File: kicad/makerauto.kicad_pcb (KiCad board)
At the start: 2 copper layers, 53.8 x 73.9 mm, 2 parts

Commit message: initial layout
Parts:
- removed the G*** at (0.00, 0.00)
- added BT1: BATT_HOLDER, makerauto:cr2032_02, B.Cu at (0.00, -9.50)
- added D1: Red, makerauto:LED-5MM, F.Cu at (0.00, 13.0)
- added D2: Grn, makerauto:LED-5MM, F.Cu at (15.0, 0.00)
- added D3: Blu, makerauto:LED-5MM, F.Cu at (-15.0, 0.00)
- added LOGO1: OPEN_HARDWARE_1, makerauto:Logo_silk_OSHW_6x6mm, B.Cu at (0.00, 23.0)
- added P1: Logo_MA, makerauto:ma_logo, F.Cu at (0.00, 0.00)
- added P2: Mirror, makerauto:MTG_3mm, F.Cu at (-24.0, -20.0)
- added P3: Mirror, makerauto:MTG_3mm, F.Cu at (24.0, -20.0)
- added P4: Pin, makerauto:MTG_0mm8, F.Cu at (-4.50, -31.0)
- added P5: Pin, makerauto:MTG_0mm8, F.Cu at (4.50, -35.0)
- added P6: Pin, makerauto:MTG_0mm8, F.Cu at (-4.50, -35.0)
- added P7: Pin, makerauto:MTG_0mm8, F.Cu at (4.50, -31.0)
- added R1: 47E, makerauto:r_0805, F.Cu at (0.00, 8.00)
- added R2: 47E, makerauto:r_0805, F.Cu at (11.0, 3.50)
- added R3: 47E, makerauto:r_0805, F.Cu at (-11.0, 3.50)
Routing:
- net /3V: track 0.00 -> 74.5 mm
- net /GND: track 0.00 -> 64.3 mm
- net /LED_grn: track 0.00 -> 10.1 mm
- net /LED_blu: track 0.00 -> 10.1 mm
- net /LED_red: track 0.00 -> 9.56 mm
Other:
- board size 53.8 x 73.9 mm -> 54.7 x 73.9 mm
- net class 0.5mm added: clearance 0.2, trace_width 0.5, via_dia 0.8, via_drill 0.4
- net class 1.0mm added: clearance 0.2, trace_width 1, via_dia 0.8, via_drill 0.4
- net class 1.5mm added: clearance 0.2, trace_width 1.5, via_dia 0.8, via_drill 0.4

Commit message: gerbers and pdf's generated
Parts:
- moved BT1 141.4 mm to (100.0, 90.5)
- moved D1 141.4 mm to (100.0, 113.0)
- moved D2 141.4 mm to (115.0, 100.0)
- moved D3 141.4 mm to (85.0, 100.0)
- moved G*** 141.4 mm to (67.1, 109.6)
- moved LOGO1 141.4 mm to (100.0, 123.0)
- moved P1 141.4 mm to (100.0, 100.0)
- moved P2 141.4 mm to (76.0, 80.0)
- moved P3 141.4 mm to (124.0, 80.0)
- moved P4 141.4 mm to (95.5, 69.0)
- moved P5 141.4 mm to (104.5, 65.0)
- moved P6 141.4 mm to (95.5, 65.0)
- moved P7 141.4 mm to (104.5, 69.0)
- moved R1 141.4 mm to (100.0, 108.0)
- moved R2 141.4 mm to (111.0, 103.5)
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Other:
- outline, holes or cut-outs redrawn

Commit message: added logos
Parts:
- added G***: LOGO, makerauto:logo_asylum, B.Cu at (88.5, 73.0)
- added G***: LOGO, makerauto:logo_autodesk, B.Cu at (112.5, 73.5)
- R1, R2, R3: moved to B.Cu
- moved LOGO1 9.00 mm to (100.0, 132.0)
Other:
- board text added: "Maker Auto : built with help from Maker's Asylum + Autodesk India"
- board text added: "SPACE FOR ETOK MARK AND CODE"
- board text added: "[+]"
- board text added: "[-]"
- board text added: "https://git.io/v6BwJ"

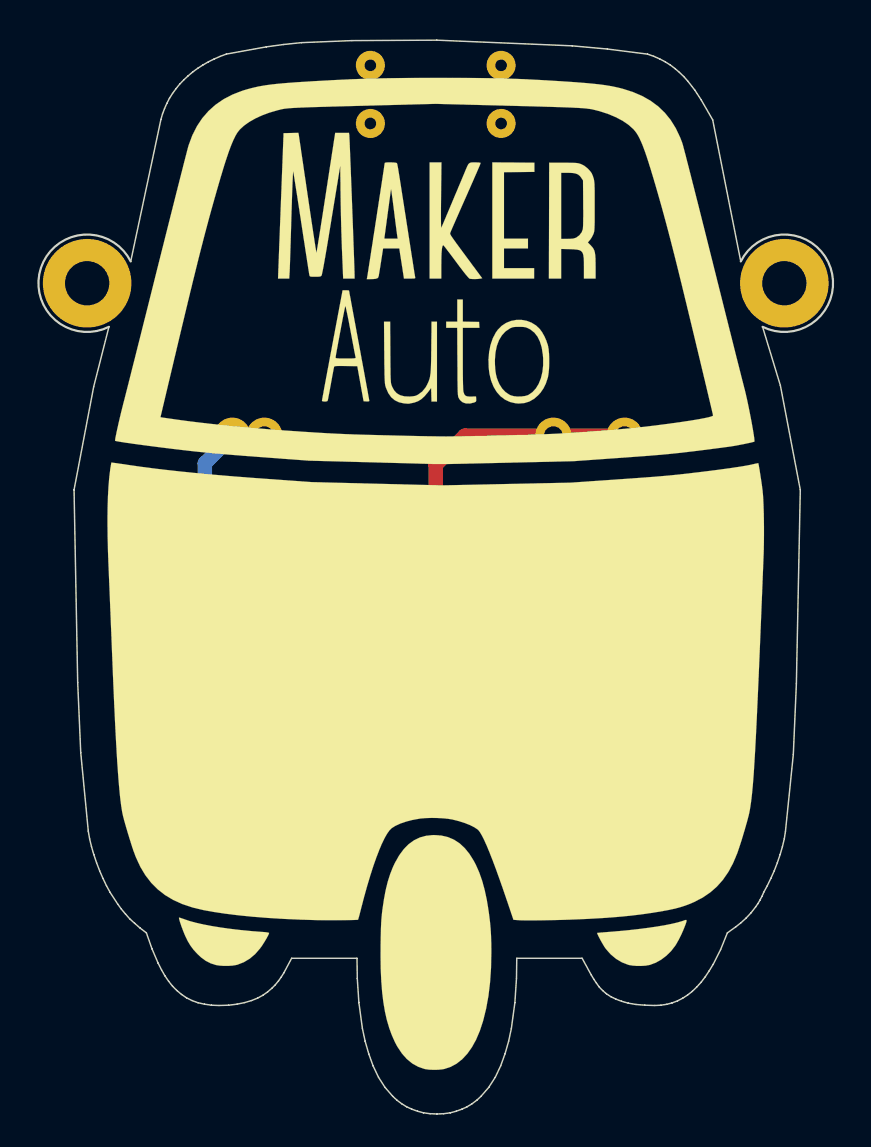
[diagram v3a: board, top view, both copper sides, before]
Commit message: added copper fill zones
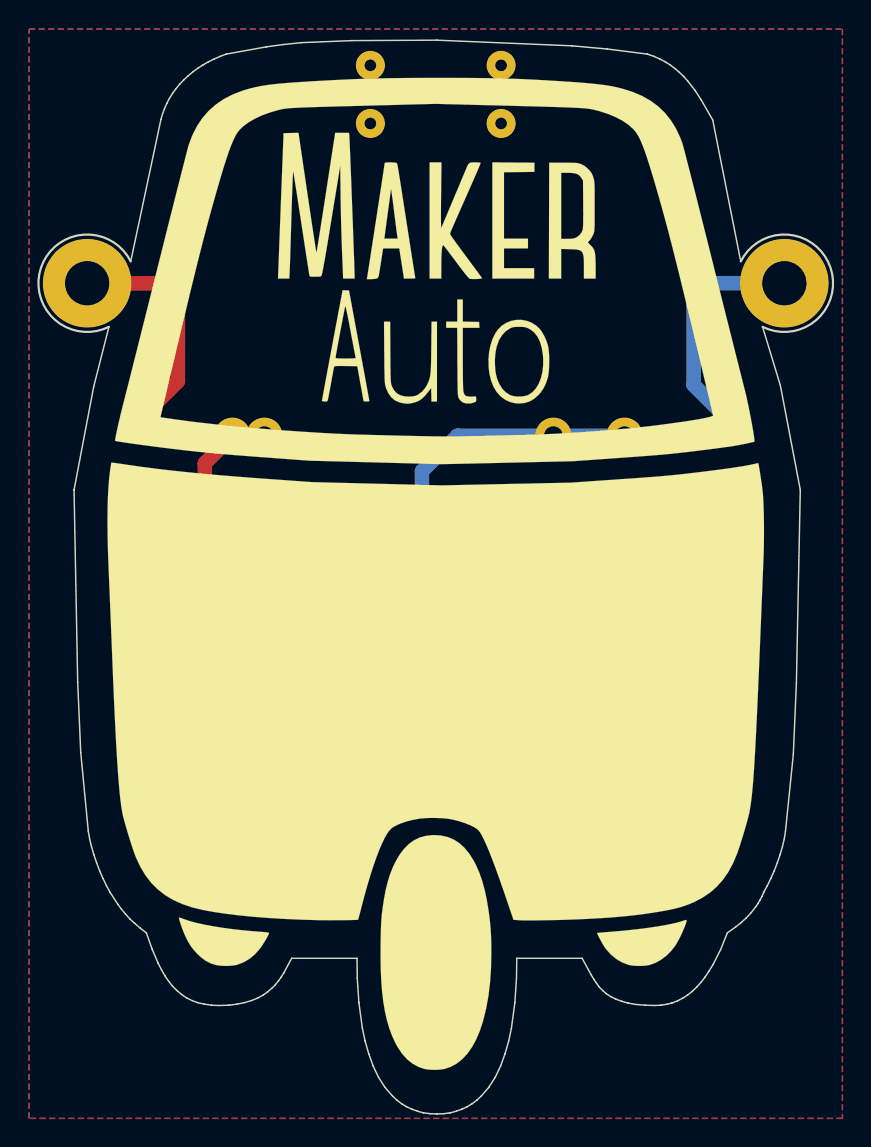
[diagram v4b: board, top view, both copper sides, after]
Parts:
- added P8: Pin, makerauto:MTG_0mm8, F.Cu at (79.5, 89.5)
- added P9: Pin, makerauto:MTG_0mm8, F.Cu at (120.5, 89.8)
- moved G*** 21.2 mm to (75.8, 129.0)
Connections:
- P2 pad 1: (no net) -> /TOP
- P3 pad 1: (no net) -> /BOT
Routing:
- net /TOP: track 0.00 -> 16.3 mm
- net /BOT: track 0.00 -> 16.3 mm
- net /LED_grn: track 10.1 -> 7.69 mm
- net /LED_blu: track 10.1 -> 7.69 mm
- net /LED_red: track 9.56 -> 7.24 mm
- net /GND: track 64.3 -> 63.4 mm
- added copper zone on B.Cu, net /BOT
- added copper zone on F.Cu, net /TOP
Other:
- board text added: "SPACE FOR ETOK CODE"
- board text removed: "SPACE FOR ETOK MARK AND CODE"

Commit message: edited back silk legend
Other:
- board text added: "makerauto.tools made at makersasylum.com"
- board text removed: "Maker Auto : built with help from Maker's Asylum + Autodesk India"
- board text removed: "https://git.io/v6BwJ"
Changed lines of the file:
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@@
     (area 72 62.5 144.750001 145.245001)
     (thickness 1.6)
-    (drawings 183)
+    (drawings 182)
     (tracks 41)
     (zones 0)
@@
   (page A4)
   (layers
-    (0 F.Cu signal)
-    (31 B.Cu signal)
+    (0 F.Cu signal hide)
+    (31 B.Cu signal hide)
     (32 B.Adhes user)
     (33 F.Adhes user)
@@
     (35 F.Paste user)
     (36 B.SilkS user)
-    (37 F.SilkS user)
+    (37 F.SilkS user hide)
     (38 B.Mask user)
     (39 F.Mask user)
@@
     (effects (font (size 1.5 1.5) (thickness 0.3)) (justify mirror))
   )
-  (gr_text "Maker Auto : built with help from\nMaker's Asylum + Autodesk India" (at 100 120.5) (layer B.SilkS)
-    (effects (font (size 1.5 1.5) (thickness 0.3)) (justify mirror))
-  )
-  (gr_text https://git.io/v6BwJ (at 100 125) (layer B.SilkS)
-    (effects (font (size 1.5 1.5) (thickness 0.3)) (justify mirror))
+  (gr_text "makerauto.tools\nmade at\nmakersasylum.com" (at 100.25 121.25) (layer B.SilkS)
+    (effects (font (size 2 2) (thickness 0.3)) (justify mirror))
   )
   (dimension 74 (width 0.3) (layer Dwgs.User)

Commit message: complete. final gerbers generated
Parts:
- moved LOGO1 0.50 mm to (100.0, 132.5)
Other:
- board text added: "git.io/v6BwJ"
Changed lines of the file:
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@@
-(kicad_pcb (version 4) (host pcbnew 4.1.0-alpha+201608101232+7015~46~ubuntu16.04.1-product)
+(kicad_pcb (version 4) (host pcbnew 4.1.0-alpha+201607210716+6990~46~ubuntu15.10.1-product)
   (general
     (links 19)
@@
     (area 72 62.5 144.750001 145.245001)
     (thickness 1.6)
-    (drawings 182)
+    (drawings 183)
     (tracks 41)
     (zones 0)
@@
   (page A4)
   (layers
-    (0 F.Cu signal hide)
-    (31 B.Cu signal hide)
+    (0 F.Cu signal)
+    (31 B.Cu signal)
     (32 B.Adhes user)
     (33 F.Adhes user)
@@
     (35 F.Paste user)
     (36 B.SilkS user)
-    (37 F.SilkS user hide)
+    (37 F.SilkS user)
     (38 B.Mask user)
     (39 F.Mask user)
@@
     (visible_elements FFFFFF7F)
     (pcbplotparams
-      (layerselection 0x010f0_ffffffff)
-      (usegerberextensions true)
-      (usegerberattributes true)
-      (excludeedgelayer true)
+      (layerselection 0x00130_ffffffff)
+      (usegerberextensions false)
+      (excludeedgelayer false)
       (linewidth 0.050800)
-      (plotframeref false)
+      (plotframeref true)
       (viasonmask false)
       (mode 1)
@@
       (plotvalue true)
       (plotinvisibletext false)
-      (padsonsilk false)
-      (subtractmaskfromsilk true)
-      (outputformat 1)
+      (padsonsilk true)
+      (subtractmaskfromsilk false)
+      (outputformat 4)
       (mirror false)
-      (drillshape 0)
+      (drillshape 2)
       (scaleselection 1)
-      (outputdirectory gerber/))
+      (outputdirectory pdf/))
   )
   (net 0 "")
@@
     (pad 2 thru_hole circle (at 0 13 90) (size 2.5 2.5) (drill 1.3) (layers *.Cu *.Mask B.SilkS)
       (net 1 /GND))
-    (model CR2032_HOR_HOLD.wrl
+    (model ${KIPRJMOD}/3d_modules/CR2032_HOR_HOLD.wrl
       (at (xyz 0 0 0))
       (scale (xyz 1 1 1))
@@
   )
   (module makerauto:Logo_silk_OSHW_6x6mm (layer B.Cu)
-    (at 100 132 180)
+    (at 100 132.5 180)
     (descr "Open Hardware Logo, 6x6mm")
     (fp_text reference LOGO1 (at 0 0 180) (layer B.SilkS) hide
@@
       (net 7 /BOT))
   )
+  (gr_text git.io/v6BwJ (at 100 129) (layer B.SilkS)
+    (effects (font (size 1 1) (thickness 0.2)) (justify mirror))
+  )
   (gr_line (start 91.5 97) (end 91.5 84) (layer B.SilkS) (width 0.2))
